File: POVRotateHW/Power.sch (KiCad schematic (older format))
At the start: 21 parts, among them P2 CONN_01X02, U1 A5970AD

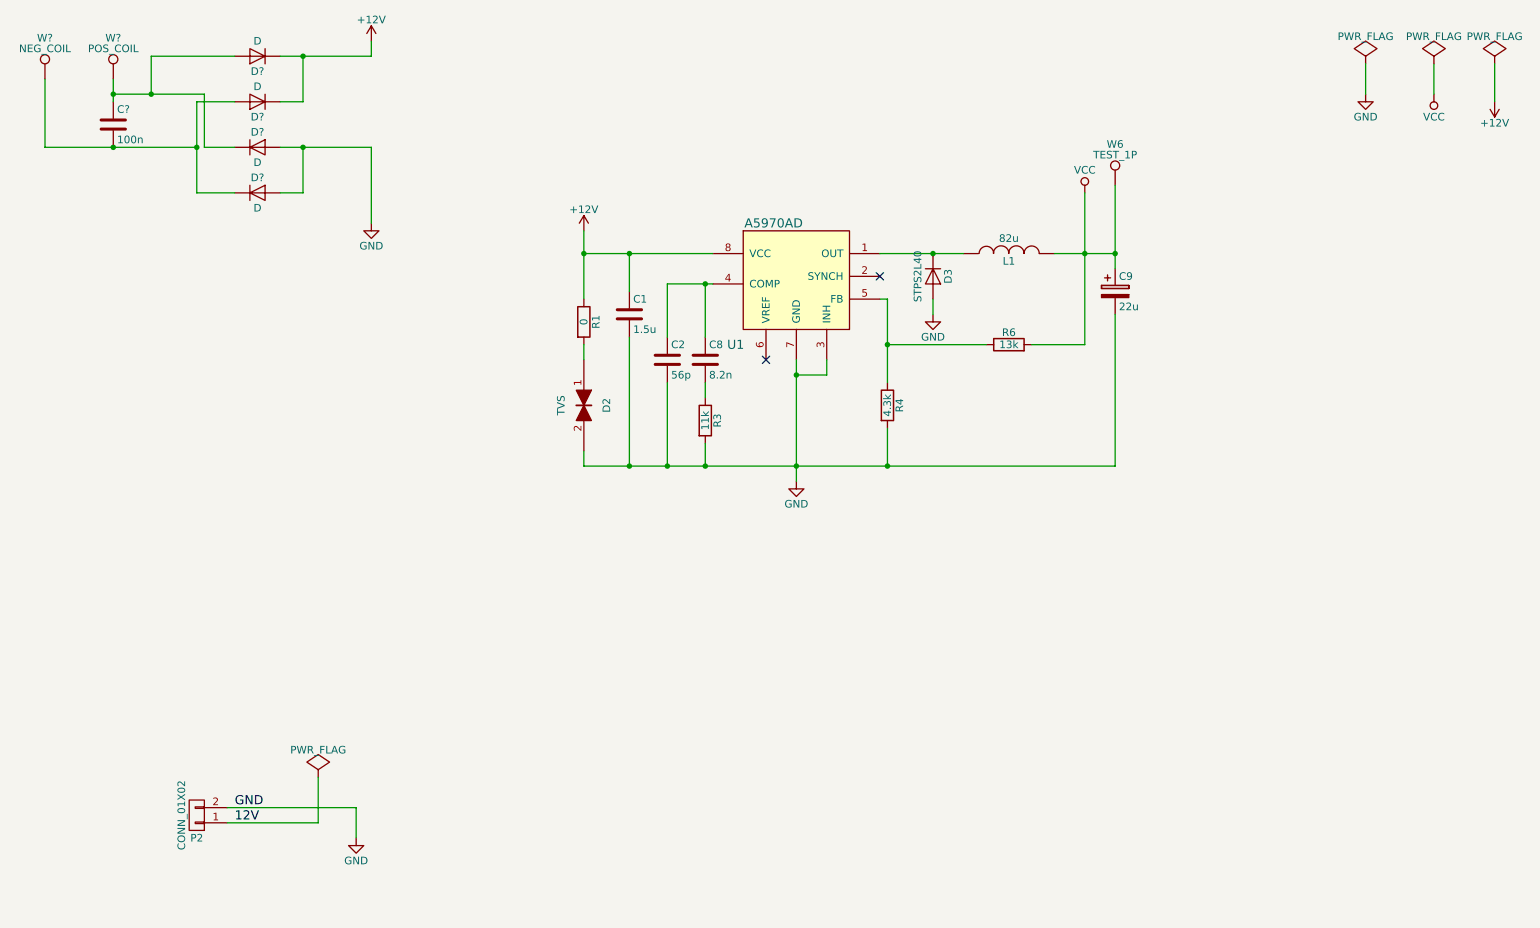
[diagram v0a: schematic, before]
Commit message: Started working on the schematic for the POV Rotate board.
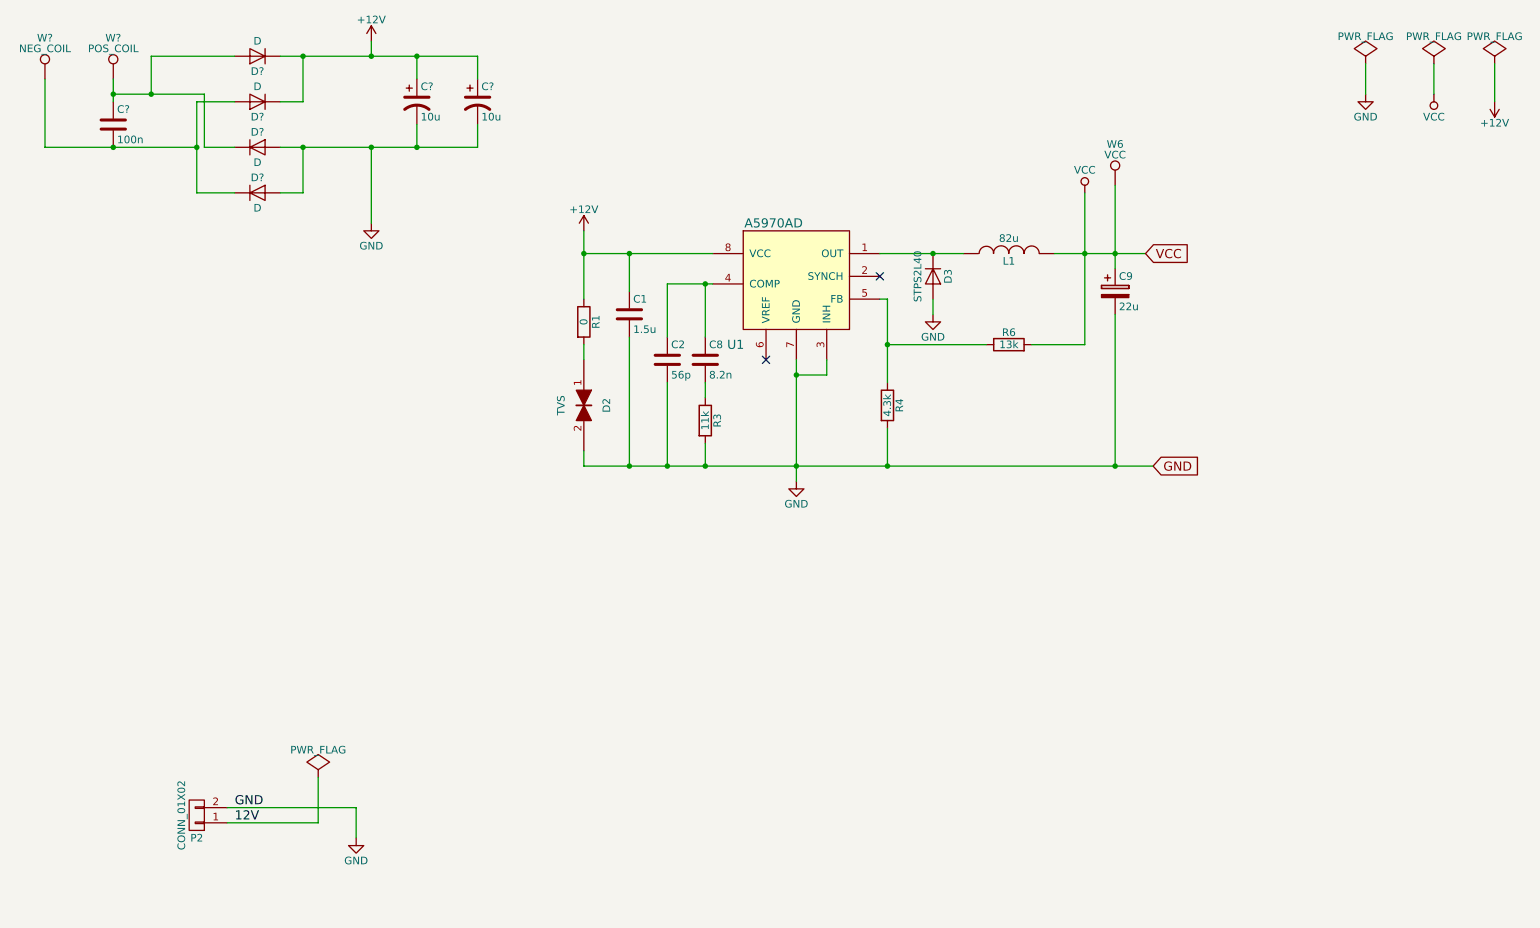
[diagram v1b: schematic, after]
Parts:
- added C? (x2): 10u, symbol CP1
- W6: value TEST_1P -> VCC
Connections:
- net +12V: now also C?.1, C?.1
- net GND: now also C?.2, C?.2
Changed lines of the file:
@@
 	1    0    0    -1
 $EndComp
-Wire Wire Line
-	9450 1350 9450 1550
-Wire Wire Line
-	9900 1350 9900 1550
 $Comp
 L VCC #PWR010
@@
 	0    -1   -1   0
 $EndComp
-Wire Wire Line
-	4300 2600 5150 2600
-Wire Wire Line
-	4300 2450 4300 2900
-Connection ~ 4300 2600
-Wire Wire Line
-	4300 3200 4300 3300
-Wire Wire Line
-	4300 3900 4300 4000
-Wire Wire Line
-	4600 2600 4600 2850
-Connection ~ 4600 2600
-Wire Wire Line
-	4600 3150 4600 4000
-Connection ~ 4600 4000
 $Comp
 L R R4
@@
 	1    0    0    -1
 $EndComp
-Wire Wire Line
-	6300 4000 6300 3750
 $Comp
 L CONN_01X02 P2
@@
 	-1   0    0    1
 $EndComp
-Wire Wire Line
-	1950 6250 2800 6250
-Wire Wire Line
-	1950 6350 2550 6350
 Text Label 2000 6250 0    60   ~ 0
 GND
@@
 	1    0    0    -1
 $EndComp
-Wire Wire Line
-	2800 6250 2800 6450
 $Comp
 L PWR_FLAG #FLG018
@@
 	-1   0    0    1
 $EndComp
-Wire Wire Line
-	10300 1600 10300 1350
 $Comp
 L A5970AD U1
@@
 	1    0    0    -1
 $EndComp
-Wire Wire Line
-	4850 2800 5150 2800
-Wire Wire Line
-	5100 2800 5100 3150
-Wire Wire Line
-	5100 3450 5100 3550
-Wire Wire Line
-	5100 4000 5100 3850
-Connection ~ 5100 4000
-Wire Wire Line
-	4850 4000 4850 3450
-Connection ~ 4850 4000
-Wire Wire Line
-	4850 3150 4850 2800
-Connection ~ 5100 2800
-Wire Wire Line
-	5700 3300 5700 4100
-Connection ~ 5700 4000
-Wire Wire Line
-	6250 2900 6300 2900
-Wire Wire Line
-	6300 2900 6300 3450
-Connection ~ 6300 4000
 $Comp
 L D D3
@@
 	0    -1   -1   0
 $EndComp
-Wire Wire Line
-	6950 3200 6300 3200
-Connection ~ 6300 3200
-Wire Wire Line
-	7600 3200 7250 3200
-Wire Wire Line
-	7600 2200 7600 3200
-Wire Wire Line
-	7400 2600 7800 2600
-Connection ~ 7600 2600
 $Comp
 L R R1
@@
 	1    0    0    -1
 $EndComp
-Wire Wire Line
-	5900 3300 5900 3400
-Wire Wire Line
-	5900 3400 5700 3400
-Connection ~ 5700 3400
-Wire Wire Line
-	4300 4000 7800 4000
 $Comp
 L GND #PWR023
@@
 	1    0    0    -1
 $EndComp
-Wire Wire Line
-	6600 3000 6600 2900
-Wire Wire Line
-	6250 2600 6800 2600
-Connection ~ 6600 2600
 $Comp
 L CP C9
@@
 	1    0    0    -1
 $EndComp
-Wire Wire Line
-	7800 4000 7800 3000
-Wire Wire Line
-	7800 2150 7800 2700
 NoConn ~ 6250 2750
 NoConn ~ 5500 3300
@@
 P 7800 2150
 F 0 "W6" H 7800 2420 50  0000 C CNN
-F 1 "TEST_1P" H 7800 2350 50  0000 C CNN
+F 1 "VCC" H 7800 2350 50  0000 C CNN
 F 2 "Measurement_Points:Measurement_Point_Round-SMD-Pad_Small" H 8000 2150 50  0001 C CNN
 F 3 "" H 8000 2150 50  0000 C CNN
@@
 	1    0    0    -1
 $EndComp
-Connection ~ 7800 2600
 $Comp
 L TEST_1P W?
@@
 	1    0    0    -1
 $EndComp
-Wire Wire Line
-	2550 6350 2550 6050
 $Comp
 L D D?
@@
 	1    0    0    -1
 $EndComp
-Wire Wire Line
-	1200 1450 1200 1600
-Wire Wire Line
-	750  1900 1750 1900
-Wire Wire Line
-	750  1900 750  1450
-Wire Wire Line
-	1200 1550 1800 1550
-Wire Wire Line
-	1450 1300 1450 1550
-Connection ~ 1200 1550
-Connection ~ 1200 1900
-Wire Wire Line
-	2000 1300 1450 1300
-Wire Wire Line
-	2000 1900 1800 1900
-Wire Wire Line
-	1800 1900 1800 1550
-Connection ~ 1450 1550
-Wire Wire Line
-	2000 1600 1750 1600
-Wire Wire Line
-	1750 1600 1750 2200
 $Comp
 L +12V #PWR?
@@
 	1    0    0    -1
 $EndComp
-Wire Wire Line
-	2900 1200 2900 1300
-Wire Wire Line
-	2900 1300 2300 1300
-Wire Wire Line
-	2300 1600 2450 1600
-Wire Wire Line
-	2450 1600 2450 1300
-Connection ~ 2450 1300
 $Comp
 L GND #PWR?
@@
 	1    0    0    -1
 $EndComp
-Wire Wire Line
-	2900 2400 2900 1900
-Wire Wire Line
-	2900 1900 2300 1900
+$Comp
+L CP1 C?
+U 1 1 5812ADCA
+P 3200 1600
+F 0 "C?" H 3225 1700 50  0000 L CNN
+F 1 "10u" H 3225 1500 50  0000 L CNN
+F 2 "" H 3200 1600 50  0000 C CNN
+F 3 "" H 3200 1600 50  0000 C CNN
+	1    3200 1600
+	1    0    0    -1
+$EndComp
+$Comp
+L CP1 C?
+U 1 1 5812AE83
+P 3600 1600
+F 0 "C?" H 3625 1700 50  0000 L CNN
+F 1 "10u" H 3625 1500 50  0000 L CNN
+F 2 "" H 3600 1600 50  0000 C CNN
+F 3 "" H 3600 1600 50  0000 C CNN
+	1    3600 1600
+	1    0    0    -1
+$EndComp
+Wire Wire Line
+	9450 1350 9450 1550
+Wire Wire Line
+	9900 1350 9900 1550
+Wire Wire Line
+	4300 2600 5150 2600
+Wire Wire Line
+	4300 2450 4300 2900
+Connection ~ 4300 2600
+Wire Wire Line
+	4300 3200 4300 3300
+Wire Wire Line
+	4300 3900 4300 4000
+Wire Wire Line
+	4600 2600 4600 2850
+Connection ~ 4600 2600
+Wire Wire Line
+	4600 3150 4600 4000
+Connection ~ 4600 4000
+Wire Wire Line
+	6300 4000 6300 3750
+Wire Wire Line
+	1950 6250 2800 6250
+Wire Wire Line
+	1950 6350 2550 6350
+Wire Wire Line
+	2800 6250 2800 6450
+Wire Wire Line
+	10300 1600 10300 1350
+Wire Wire Line
+	4850 2800 5150 2800
+Wire Wire Line
+	5100 2800 5100 3150
+Wire Wire Line
+	5100 3450 5100 3550
+Wire Wire Line
+	5100 4000 5100 3850
+Connection ~ 5100 4000
+Wire Wire Line
+	4850 4000 4850 3450
+Connection ~ 4850 4000
+Wire Wire Line
+	4850 3150 4850 2800
+Connection ~ 5100 2800
+Wire Wire Line
+	5700 3300 5700 4100
+Connection ~ 5700 4000
+Wire Wire Line
+	6250 2900 6300 2900
+Wire Wire Line
+	6300 2900 6300 3450
+Connection ~ 6300 4000
+Wire Wire Line
+	6950 3200 6300 3200
+Connection ~ 6300 3200
+Wire Wire Line
+	7600 3200 7250 3200
+Wire Wire Line
+	7600 2200 7600 3200
+Wire Wire Line
+	7400 2600 8000 2600
+Connection ~ 7600 2600
+Wire Wire Line
+	5900 3300 5900 3400
+Wire Wire Line
+	5900 3400 5700 3400
+Connection ~ 5700 3400
+Wire Wire Line
+	4300 4000 8050 4000
+Wire Wire Line
+	6600 3000 6600 2900
+Wire Wire Line
+	6250 2600 6800 2600
+Connection ~ 6600 2600
+Wire Wire Line
+	7800 4000 7800 3000
+Wire Wire Line
+	7800 2150 7800 2700
+Connection ~ 7800 2600
+Wire Wire Line
+	2550 6350 2550 6050
+Wire Wire Line
+	1200 1450 1200 1600
+Wire Wire Line
+	750  1900 1750 1900
+Wire Wire Line
+	750  1900 750  1450
+Wire Wire Line
+	1200 1550 1800 1550
+Wire Wire Line
+	1450 1300 1450 1550
+Connection ~ 1200 1550
+Connection ~ 1200 1900
+Wire Wire Line
+	2000 1300 1450 1300
+Wire Wire Line
+	2000 1900 1800 1900
+Wire Wire Line
+	1800 1900 1800 1550
+Connection ~ 1450 1550
+Wire Wire Line
+	2000 1600 1750 1600
+Wire Wire Line
+	1750 1600 1750 2200
+Wire Wire Line
+	2900 1300 2900 1200
+Wire Wire Line
+	2300 1300 3600 1300
+Wire Wire Line
+	2300 1600 2450 1600
+Wire Wire Line
+	2450 1600 2450 1300
+Connection ~ 2450 1300
+Wire Wire Line
+	2900 1900 2900 2400
+Wire Wire Line
+	2300 1900 3600 1900
 Wire Wire Line
 	2300 2200 2450 2200
@@
 	1750 2200 2000 2200
 Connection ~ 1750 1900
+Wire Wire Line
+	3200 1300 3200 1450
+Connection ~ 2900 1300
+Wire Wire Line
+	3600 1300 3600 1450
+Connection ~ 3200 1300
+Connection ~ 2900 1900
+Connection ~ 3200 1900
+Wire Wire Line
+	3200 1900 3200 1750
+Wire Wire Line
+	3600 1900 3600 1750
+Text GLabel 8000 2600 2    60   Input ~ 0
+VCC
+Text GLabel 8050 4000 2    60   Input ~ 0
+GND
+Connection ~ 7800 4000
 $EndSCHEMATC

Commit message: Finished the schematic for the POVRotate system, started on layout.
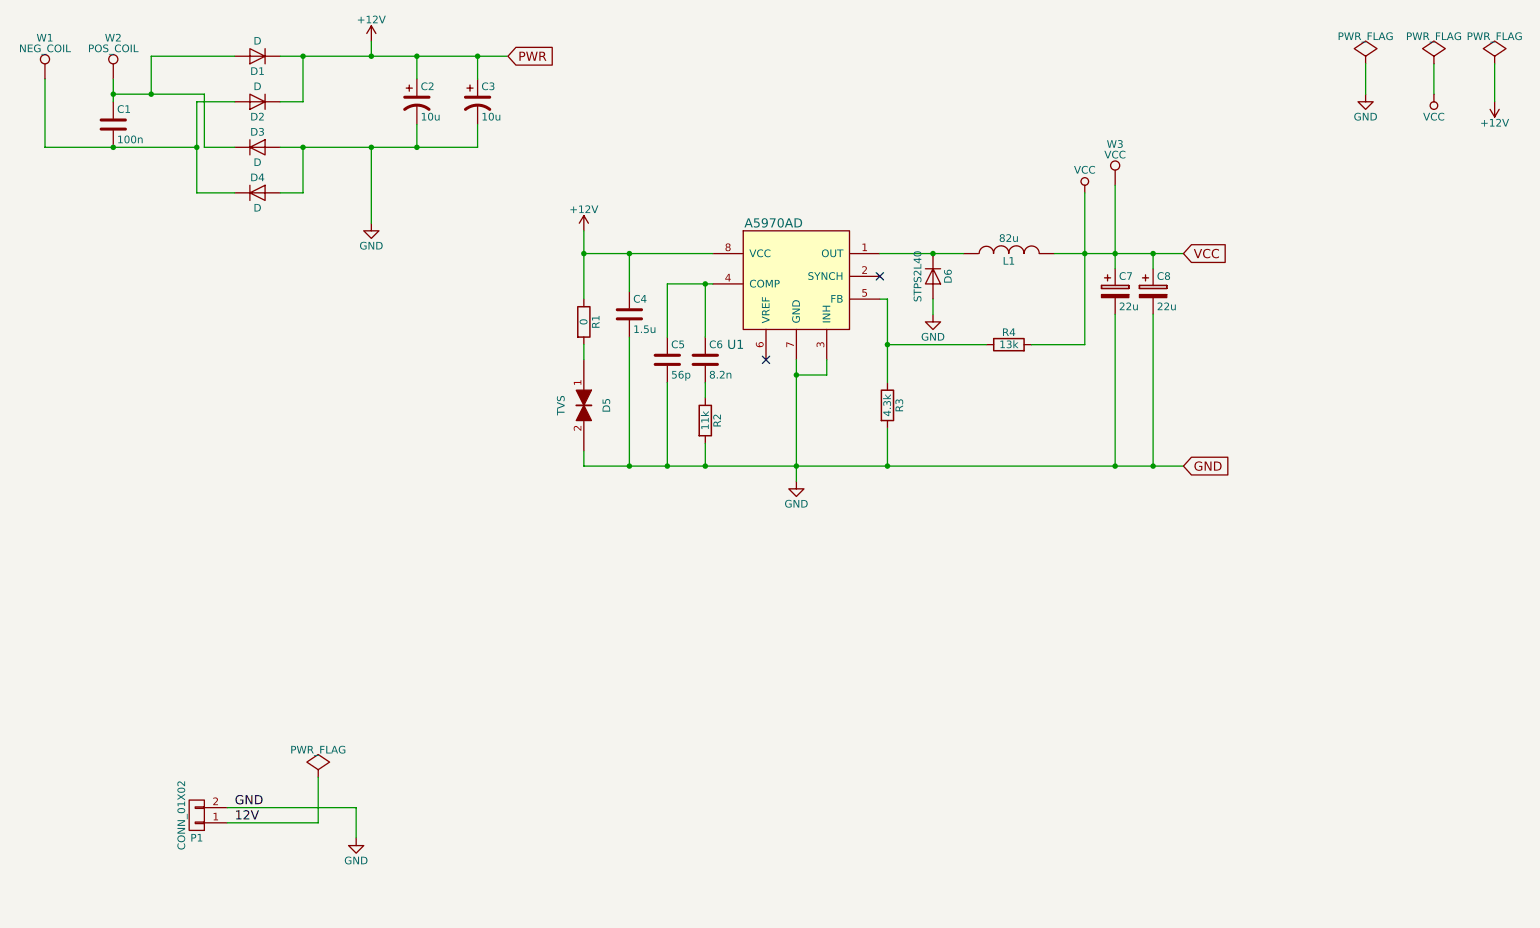
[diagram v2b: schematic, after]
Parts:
- removed C?: 10u, symbol CP1
- removed D? (x3): D, symbol D
- added C3: 10u, symbol CP1
- added C8: 22u, SMD_Packages:SMD-1210_Pol, symbol CP
- added D2, D3, D4: D, symbol D
- C2: renamed from C?; DIGIKEY (none) -> PCE5022CT-ND
- D1: renamed from D?; DIGIKEY (none) -> 497-5574-1-ND
- U1: footprint myfootprint:SO-8 -> (none)
- gave numbers to parts that had none: 3
- renumbered C1 to C4, C2 to C5, C8 to C6, C9 to C7, D2 to D5, D3 to D6, P2 to P1, R3 to R2, R4 to R3, R6 to R4, W6 to W3
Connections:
- net +12V: now also C3.1, D2.1 (K)
- net GND: now also C3.2, C8.2, D3.2 (A), D4.2 (A)
- net VCC: now also C8.1
- net at C1.1, D1.2 (A), W2.1: now also D3.1 (K)
- net at C1.2, W1.1: now also D2.2 (A), D4.1 (K)

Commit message: Started work on the POV Rotate layout.
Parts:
- C1: footprint (none) -> Capacitors_SMD:C_1210_HandSoldering
- C2, C3: footprint (none) -> Capacitors_SMD:c_elec_5x5.8
- D1, D2, D3, D4: footprint (none) -> Diodes_SMD:SMB_Handsoldering
- L1: footprint myfootprint:TDK_Inductor_12.95x9.4x5.08 -> KicadLibrary:TDK_inductor_12.95x9.4x8.08
- U1: footprint (none) -> SMD_Packages:SOIC-8-N
- W1, W2: footprint (none) -> Mounting_Holes:MountingHole_3.2mm_M3_DIN965_Pad
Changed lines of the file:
@@
 F 0 "L1" V 7050 2600 50  0000 C CNN
 F 1 "82u" V 7200 2600 50  0000 C CNN
-F 2 "myfootprint:TDK_Inductor_12.95x9.4x5.08" H 7100 2600 50  0001 C CNN
+F 2 "KicadLibrary:TDK_inductor_12.95x9.4x8.08" H 7100 2600 50  0001 C CNN
 F 3 "" H 7100 2600 50  0000 C CNN
 F 4 "495-2686-1-ND" V 7100 2600 60  0001 C CNN "Digikey"
@@
 F 0 "W2" H 1200 1720 50  0000 C CNN
 F 1 "POS_COIL" H 1200 1650 50  0000 C CNN
-F 2 "" H 1400 1450 50  0000 C CNN
+F 2 "Mounting_Holes:MountingHole_3.2mm_M3_DIN965_Pad" H 1400 1450 50  0001 C CNN
 F 3 "" H 1400 1450 50  0000 C CNN
 	1    1200 1450
@@
 F 0 "W1" H 750 1720 50  0000 C CNN
 F 1 "NEG_COIL" H 750 1650 50  0000 C CNN
-F 2 "" H 950 1450 50  0000 C CNN
+F 2 "Mounting_Holes:MountingHole_3.2mm_M3_DIN965_Pad" H 950 1450 50  0001 C CNN
 F 3 "" H 950 1450 50  0000 C CNN
 	1    750  1450
@@
 F 0 "D1" H 2150 1400 50  0000 C CNN
 F 1 "D" H 2150 1200 50  0000 C CNN
-F 2 "" H 2150 1300 50  0000 C CNN
+F 2 "Diodes_SMD:SMB_Handsoldering" H 2150 1300 50  0001 C CNN
 F 3 "" H 2150 1300 50  0000 C CNN
 F 4 "497-5574-1-ND" H 2150 1300 60  0001 C CNN "DIGIKEY"
@@
 F 0 "C1" H 1225 1850 50  0000 L CNN
 F 1 "100n" H 1225 1650 50  0000 L CNN
-F 2 "" H 1238 1600 50  0000 C CNN
+F 2 "Capacitors_SMD:C_1210_HandSoldering" H 1238 1600 50  0001 C CNN
 F 3 "" H 1200 1750 50  0000 C CNN
 	1    1200 1750
@@
 F 0 "C2" H 3225 1700 50  0000 L CNN
 F 1 "10u" H 3225 1500 50  0000 L CNN
-F 2 "" H 3200 1600 50  0000 C CNN
+F 2 "Capacitors_SMD:c_elec_5x5.8" H 3200 1600 50  0001 C CNN
 F 3 "" H 3200 1600 50  0000 C CNN
 F 4 "PCE5022CT-ND" H 3200 1600 60  0001 C CNN "DIGIKEY"
@@
 F 0 "D2" H 2150 1700 50  0000 C CNN
 F 1 "D" H 2150 1500 50  0000 C CNN
-F 2 "" H 2150 1600 50  0000 C CNN
+F 2 "Diodes_SMD:SMB_Handsoldering" H 2150 1600 50  0001 C CNN
 F 3 "" H 2150 1600 50  0000 C CNN
 F 4 "497-5574-1-ND" H 2150 1600 60  0001 C CNN "DIGIKEY"
@@
 F 0 "D3" H 2150 2000 50  0000 C CNN
 F 1 "D" H 2150 1800 50  0000 C CNN
-F 2 "" H 2150 1900 50  0000 C CNN
+F 2 "Diodes_SMD:SMB_Handsoldering" H 2150 1900 50  0001 C CNN
 F 3 "" H 2150 1900 50  0000 C CNN
 F 4 "497-5574-1-ND" H 2150 1900 60  0001 C CNN "DIGIKEY"
@@
 F 0 "D4" H 2150 2300 50  0000 C CNN
 F 1 "D" H 2150 2100 50  0000 C CNN
-F 2 "" H 2150 2200 50  0000 C CNN
+F 2 "Diodes_SMD:SMB_Handsoldering" H 2150 2200 50  0001 C CNN
 F 3 "" H 2150 2200 50  0000 C CNN
 F 4 "497-5574-1-ND" H 2150 2200 60  0001 C CNN "DIGIKEY"
@@
 F 0 "C3" H 3625 1700 50  0000 L CNN
 F 1 "10u" H 3625 1500 50  0000 L CNN
-F 2 "" H 3600 1600 50  0000 C CNN
+F 2 "Capacitors_SMD:c_elec_5x5.8" H 3600 1600 50  0001 C CNN
 F 3 "" H 3600 1600 50  0000 C CNN
 F 4 "PCE5022CT-ND" H 3600 1600 60  0001 C CNN "DIGIKEY"
@@
 F 0 "U1" H 5300 2200 60  0000 C CNN
 F 1 "A5970AD" H 5550 3000 60  0000 C CNN
-F 2 "" H 5700 2700 60  0000 C CNN
+F 2 "SMD_Packages:SOIC-8-N" H 5700 2700 60  0001 C CNN
 F 3 "" H 5700 2700 60  0000 C CNN
 F 4 "497-10183-1-ND" H 5700 2700 60  0001 C CNN "DIGIKEY"

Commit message: Moved parts around.
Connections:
- net 12V is gone; now on net +12V: P1.1 (P1)
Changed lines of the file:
@@
 Connection ~ 7800 2600
 Wire Wire Line
-	2550 6350 2550 6050
+	2550 6050 2550 6900
 Wire Wire Line
 	1200 1450 1200 1600
@@
 	1    0    0    -1
 $EndComp
+Text GLabel 2700 6900 2    60   Input ~ 0
+PWR
+Wire Wire Line
+	2550 6900 2700 6900
+Connection ~ 2550 6350
 $EndSCHEMATC

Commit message: Starting layout on the new design.
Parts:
- removed P1: CONN_01X02, Socket_Strips:Socket_Strip_Straight_1x02, symbol CONN_01X02
- added W? (x2): TEST_1P, symbol TEST_1P
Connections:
- net +12V: now also W?.1
- net GND: now also W?.1
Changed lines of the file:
@@
 $EndComp
-$Comp
-L CONN_01X02 P1
-U 1 1 57E8BBF6
-P 1750 6300
-F 0 "P1" H 1750 6450 50  0000 C CNN
-F 1 "CONN_01X02" V 1850 6300 50  0000 C CNN
-F 2 "Socket_Strips:Socket_Strip_Straight_1x02" H 1750 6300 50  0001 C CNN
-F 3 "" H 1750 6300 50  0000 C CNN
-	1    1750 6300
-	-1   0    0    1
-$EndComp
-Text Label 2000 6250 0    60   ~ 0
-GND
-Text Label 2000 6350 0    60   ~ 0
-12V
 $Comp
 L GND #PWR08
 U 1 1 57E8C888
-P 2800 6450
-F 0 "#PWR08" H 2800 6200 50  0001 C CNN
-F 1 "GND" H 2800 6300 50  0000 C CNN
-F 2 "" H 2800 6450 50  0000 C CNN
-F 3 "" H 2800 6450 50  0000 C CNN
-	1    2800 6450
+P 2150 6300
+F 0 "#PWR08" H 2150 6050 50  0001 C CNN
+F 1 "GND" H 2150 6150 50  0000 C CNN
+F 2 "" H 2150 6300 50  0000 C CNN
+F 3 "" H 2150 6300 50  0000 C CNN
+	1    2150 6300
 	1    0    0    -1
 $EndComp
@@
 L PWR_FLAG #FLG012
 U 1 1 581282A9
-P 2550 6050
-F 0 "#FLG012" H 2550 6145 50  0001 C CNN
-F 1 "PWR_FLAG" H 2550 6230 50  0000 C CNN
-F 2 "" H 2550 6050 50  0000 C CNN
-F 3 "" H 2550 6050 50  0000 C CNN
-	1    2550 6050
+P 1350 6200
+F 0 "#FLG012" H 1350 6295 50  0001 C CNN
+F 1 "PWR_FLAG" H 1350 6380 50  0000 C CNN
+F 2 "" H 1350 6200 50  0000 C CNN
+F 3 "" H 1350 6200 50  0000 C CNN
+	1    1350 6200
 	1    0    0    -1
 $EndComp
@@
 	6300 4000 6300 3750
 Wire Wire Line
-	1950 6250 2800 6250
-Wire Wire Line
-	1950 6350 2550 6350
-Wire Wire Line
-	2800 6250 2800 6450
-Wire Wire Line
 	10300 1600 10300 1350
 Wire Wire Line
@@
 	7800 2150 7800 2700
 Connection ~ 7800 2600
-Wire Wire Line
-	2550 6050 2550 6900
 Wire Wire Line
 	1200 1450 1200 1600
@@
 	1    0    0    -1
 $EndComp
-Text GLabel 2700 6900 2    60   Input ~ 0
+Text GLabel 1200 6350 0    60   Input ~ 0
 PWR
-Wire Wire Line
-	2550 6900 2700 6900
-Connection ~ 2550 6350
+$Comp
+L TEST_1P W?
+U 1 1 584868C9
+P 2150 6200
+F 0 "W?" H 2150 6470 50  0000 C CNN
+F 1 "TEST_1P" H 2150 6400 50  0000 C CNN
+F 2 "" H 2350 6200 50  0000 C CNN
+F 3 "" H 2350 6200 50  0000 C CNN
+	1    2150 6200
+	1    0    0    -1
+$EndComp
+$Comp
+L TEST_1P W?
+U 1 1 58486C45
+P 1650 6250
+F 0 "W?" H 1650 6520 50  0000 C CNN
+F 1 "TEST_1P" H 1650 6450 50  0000 C CNN
+F 2 "" H 1850 6250 50  0000 C CNN
+F 3 "" H 1850 6250 50  0000 C CNN
+	1    1650 6250
+	1    0    0    -1
+$EndComp
+Wire Wire Line
+	1650 6350 1650 6250
+Wire Wire Line
+	1200 6350 1650 6350
+Wire Wire Line
+	1350 6350 1350 6200
+Connection ~ 1350 6350
+Wire Wire Line
+	2150 6200 2150 6300
 $EndSCHEMATC
